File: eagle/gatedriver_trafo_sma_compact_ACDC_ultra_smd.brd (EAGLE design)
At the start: 101.9 x 165.1 mm, 90 parts, among them K1 G5V-2, X4 BU-SMA-V

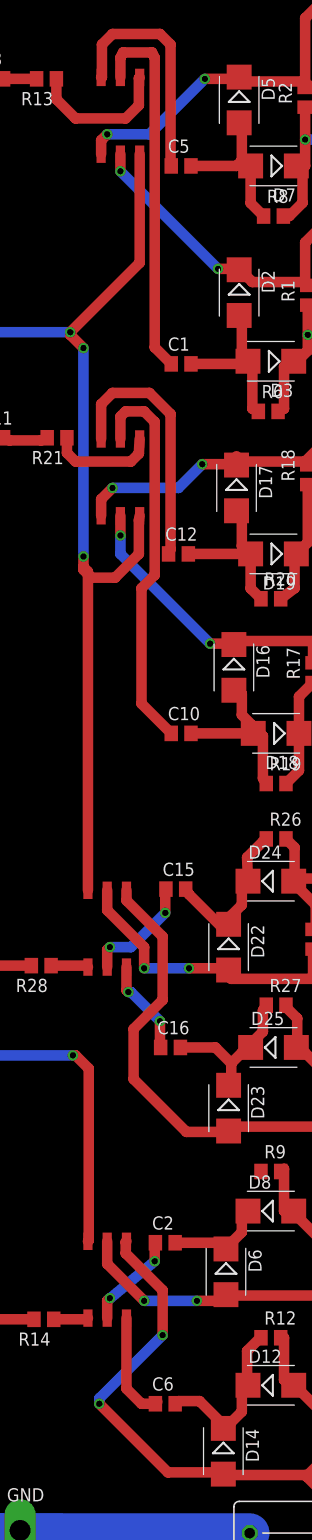
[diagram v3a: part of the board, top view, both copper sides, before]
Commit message: add tplace trafo
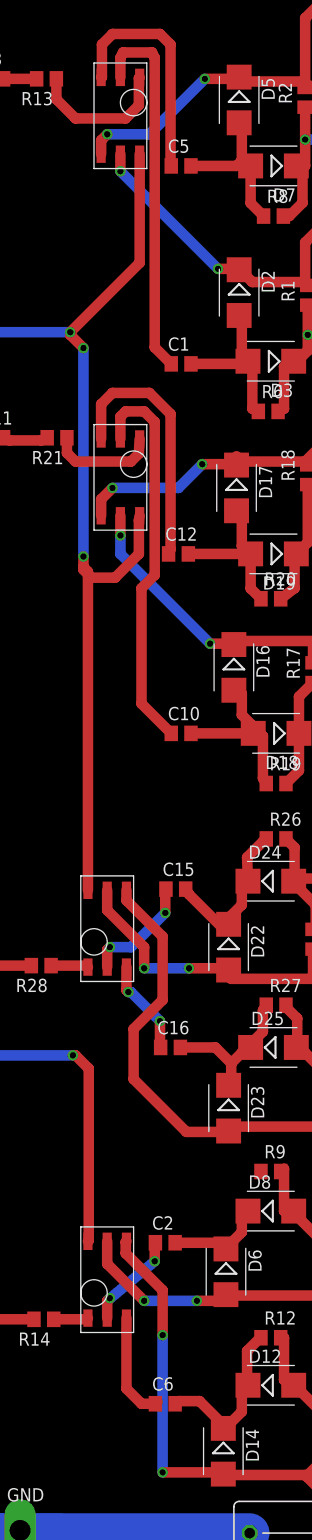
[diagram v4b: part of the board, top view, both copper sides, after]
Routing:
- net N$24: track 89.3 -> 84.5 mm
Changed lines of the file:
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@@
 <wire x1="75.184" y1="8.382" x2="74.93" y2="7.874" width="1.016" layer="1"/>
 <wire x1="88.392" y1="7.874" x2="87.884" y2="7.874" width="1.016" layer="16"/>
-<wire x1="50.292" y1="20.32" x2="56.896" y2="13.716" width="1.016" layer="1"/>
-<wire x1="56.896" y1="13.716" x2="62.5155" y2="13.716" width="1.016" layer="1"/>
+<wire x1="56.388" y1="13.716" x2="62.5155" y2="13.716" width="1.016" layer="1"/>
 <wire x1="62.5155" y1="13.716" x2="62.74119375" y2="13.49030625" width="1.016" layer="1"/>
 <wire x1="75.463" y1="18.745" x2="75.133" y2="18.745" width="1.016" layer="1"/>
@@
 <wire x1="71.628" y1="14.732" x2="70.231" y2="13.335" width="1.016" layer="1"/>
 <wire x1="87.884" y1="7.874" x2="87.884" y2="13.97" width="1.4224" layer="1"/>
-<via x="50.292" y="20.32" extent="1-16" drill="0.6" shape="square"/>
-<wire x1="50.292" y1="20.32" x2="50.292" y2="20.828" width="1.016" layer="16"/>
-<wire x1="50.292" y1="20.828" x2="56.388" y2="26.924" width="1.016" layer="16"/>
+<via x="56.388" y="13.716" extent="1-16" drill="0.6" shape="square"/>
+<wire x1="56.388" y1="13.716" x2="56.388" y2="26.924" width="1.016" layer="16"/>
 <via x="56.388" y="26.924" extent="1-16" drill="0.6" shape="square"/>
 <wire x1="56.388" y1="26.924" x2="56.388" y2="31.242" width="1.016" layer="1"/>

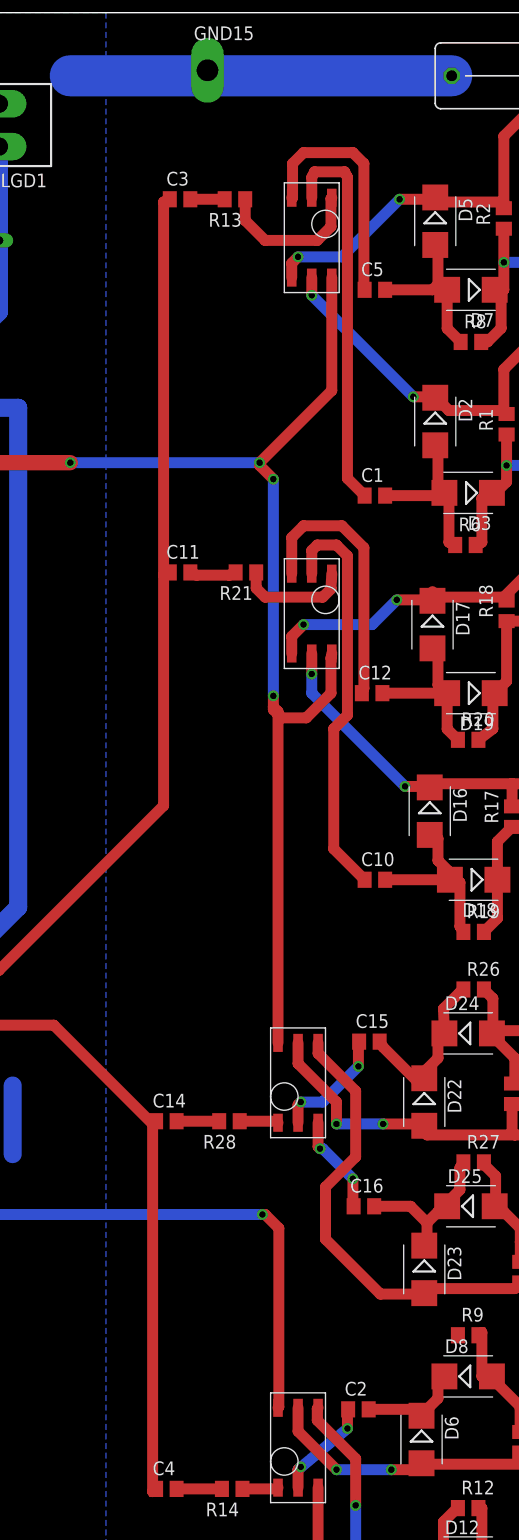
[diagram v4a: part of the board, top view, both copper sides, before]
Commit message: Fix negative rail problems
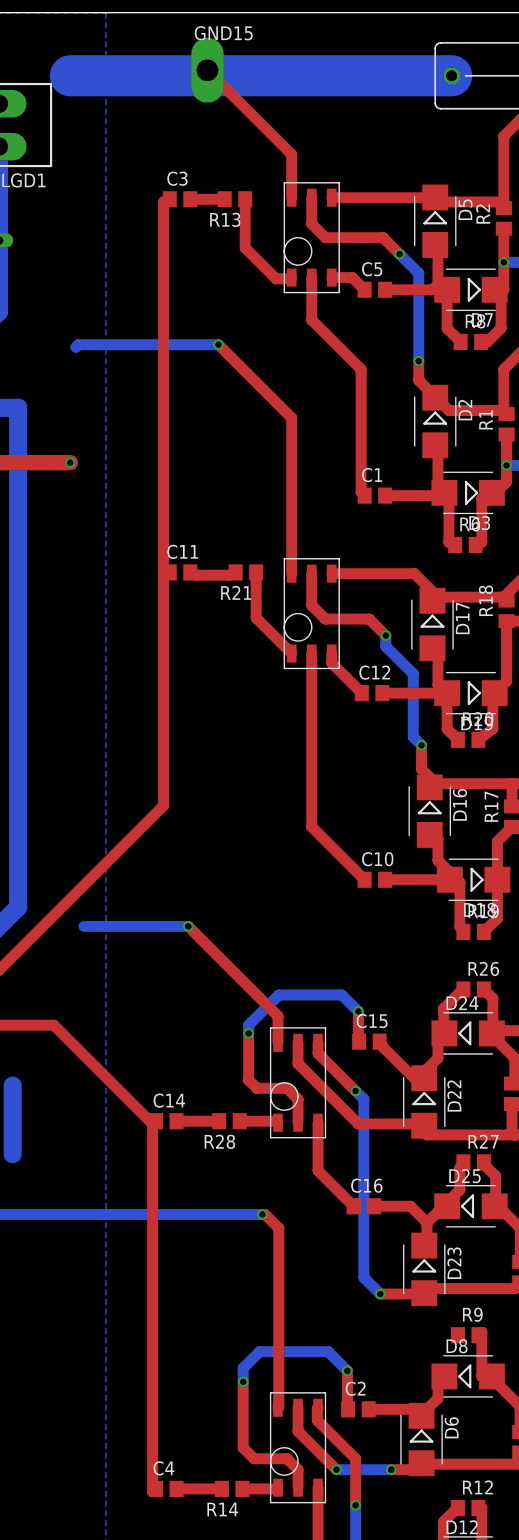
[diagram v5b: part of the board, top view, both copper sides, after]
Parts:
- D14, D16, D17, D2, D22, D23, D5, D6: value 4742 -> 1SMB5918BT3G
- R10, R11, R15, R16, R22, R23, R4, R7: value 1M -> 10M
- turned U$1 to 90 degrees
- turned U$8 to 90 degrees
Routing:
- net GND: track 272.9 -> 246.7 mm, vias 6 -> 5
- net N$29: track 24.8 -> 4.82 mm
- net N$22: track 10.1 -> 29.6 mm
- net N$7: track 22.4 -> 3.51 mm
- net N$40: track 11.0 -> 27.3 mm
- net N$28: track 37.8 -> 23.0 mm
- net N$5: track 35.9 -> 22.2 mm
- net N$18: track 102.3 -> 111.9 mm
- net N$33: track 97.3 -> 105.7 mm
- net N$17: track 88.1 -> 80.6 mm, vias 2 -> 0
- net N$32: track 103.0 -> 97.0 mm, vias 4 -> 2
- net N$3: track 13.9 -> 10.0 mm
- net N$51: track 100.9 -> 98.6 mm, vias 0 -> 2
- net N$37: track 10.5 -> 8.87 mm
- net N$46: track 93.7 -> 92.5 mm, vias 2 -> 0
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
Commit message: Fix gate driver missing trace, make changes to code for wei
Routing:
- net N$25: track 10.0 -> 14.3 mm
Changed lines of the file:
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@@
 <wire x1="64.008" y1="38.862" x2="64.602" y2="38.862" width="1.016" layer="1"/>
 <wire x1="62.992" y1="35.814" x2="62.484" y2="35.22" width="1.016" layer="1"/>
-<wire x1="64.602" y1="38.862" x2="65.852" y2="42.672" width="0" layer="19" extent="1-1"/>
+<wire x1="64.602" y1="38.862" x2="64.602" y2="41.422" width="1.016" layer="1"/>
+<wire x1="64.602" y1="41.422" x2="65.852" y2="42.672" width="1.016" layer="1"/>
 </signal>
 <signal name="N$27">

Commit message: Component value changes for gate driver with new fets (VN2450)
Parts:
- C1, C10, C11, C12, C14, C15, C16, C2, C3, C4, C5, C6: value .22u -> 1u
- R13, R14, R28: value 50 -> 10
- R21: value 50 -> 1u
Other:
- board text added: "Requires conformal coating"
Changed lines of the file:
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@@
 <hole x="6.858" y="4.572" drill="3.7973"/>
 <hole x="5.842" y="159.258" drill="3.7973"/>
+<text x="2.032" y="40.386" size="1.778" layer="21">Requires conformal coating</text>
 </plain>
 <attributes>
@@
 <attribute name="OC_FARNELL" value="unknown" x="23.368" y="154.686" size="1.778" layer="27" rot="R90" display="off"/>
 </element>
-<element name="C1" library="resistor" package="C0805" value=".22u" x="58.166" y="120.396"/>
-<element name="C3" library="resistor" package="C0805" value=".22u" x="40.132" y="147.828"/>
+<element name="C1" library="resistor" package="C0805" value="1u" x="58.166" y="120.396"/>
+<element name="C3" library="resistor" package="C0805" value="1u" x="40.132" y="147.828"/>
 <element name="U$3" library="texas" package="DIL08" value="UCC27425" x="18.288" y="75.438" rot="R270"/>
-<element name="C4" library="resistor" package="C0805" value=".22u" x="38.862" y="28.448"/>
+<element name="C4" library="resistor" package="C0805" value="1u" x="38.862" y="28.448"/>
 <element name="K1" library="relay" package="G5V-2" value="G5V-2" x="18.288" y="127.254" rot="R270">
 <attribute name="OC_NEWARK" value="78K5703" x="18.288" y="127.254" size="1.778" layer="27" rot="R270" display="off"/>
@@
 <element name="D11" library="diode" package="DO35-10" value="1N4148DO35-10" x="18.288" y="144.018"/>
 <element name="U$1" library="trafo" package="SMD6" value="DA-2320SMD6" x="52.324" y="144.272" rot="R90"/>
-<element name="C5" library="resistor" package="C0805" value=".22u" x="58.166" y="139.446"/>
+<element name="C5" library="resistor" package="C0805" value="1u" x="58.166" y="139.446"/>
 <element name="R4" library="rcl" package="R2512" value="10M" x="84.328" y="146.05" rot="R270"/>
 <element name="R7" library="rcl" package="R2512" value="10M" x="84.074" y="127.254" rot="R270"/>
-<element name="C2" library="resistor" package="C0805" value=".22u" x="56.642" y="35.814"/>
+<element name="C2" library="resistor" package="C0805" value="1u" x="56.642" y="35.814"/>
 <element name="U$2" library="transistor-fet" package="SOT89-BCE" value="VN2450" x="77.216" y="33.274" rot="R180"/>
 <element name="U$6" library="transistor-fet" package="SOT89-BCE" value="VN2450" x="76.962" y="16.764" rot="R180"/>
 <element name="U$7" library="trafo" package="SMD6" value="DA-2320SMD6" x="51.054" y="32.258" rot="R90"/>
-<element name="C6" library="resistor" package="C0805" value=".22u" x="56.642" y="20.32"/>
+<element name="C6" library="resistor" package="C0805" value="1u" x="56.642" y="20.32"/>
 <element name="R10" library="rcl" package="R2512" value="10M" x="83.82" y="34.798" rot="R90"/>
 <element name="R11" library="rcl" package="R2512" value="10M" x="83.82" y="17.78" rot="R90"/>
@@
 <element name="R9" library="rcl" package="R0805" value="10" x="66.802" y="42.672"/>
 <element name="R12" library="rcl" package="R0805" value="10" x="66.802" y="26.67"/>
-<element name="R13" library="rcl" package="R0805" value="50" x="45.212" y="147.828" rot="R180"/>
-<element name="R14" library="rcl" package="R0805" value="50" x="44.958" y="28.448" rot="R180"/>
+<element name="R13" library="rcl" package="R0805" value="10" x="45.212" y="147.828" rot="R180"/>
+<element name="R14" library="rcl" package="R0805" value="10" x="44.958" y="28.448" rot="R180"/>
 <element name="C8" library="resistor" package="C102-064X133" value="10p" x="70.358" y="159.258" rot="R180"/>
 <element name="HV2" library="testpad" package="P1-20Y" value="TPPAD1-20Y" x="87.884" y="7.874">
@@
 <attribute name="TP_SIGNAL_NAME" value="" x="74.676" y="92.964" size="1.778" layer="27" display="off"/>
 </element>
-<element name="C10" library="resistor" package="C0805" value=".22u" x="58.166" y="84.836"/>
-<element name="C11" library="resistor" package="C0805" value=".22u" x="40.132" y="113.284"/>
+<element name="C10" library="resistor" package="C0805" value="1u" x="58.166" y="84.836"/>
+<element name="C11" library="resistor" package="C0805" value="1u" x="40.132" y="113.284"/>
 <element name="U$8" library="trafo" package="SMD6" value="DA-2320SMD6" x="52.324" y="109.474" rot="R90"/>
-<element name="C12" library="resistor" package="C0805" value=".22u" x="57.912" y="102.108"/>
+<element name="C12" library="resistor" package="C0805" value="1u" x="57.912" y="102.108"/>
 <element name="R15" library="rcl" package="R2512" value="10M" x="84.074" y="110.236" rot="R90"/>
 <element name="R16" library="rcl" package="R2512" value="10M" x="84.074" y="90.678" rot="R90"/>
@@
 <element name="R19" library="rcl" package="R0805" value="10" x="67.31" y="80.01"/>
 <element name="R20" library="rcl" package="R0805" value="10" x="66.802" y="97.79"/>
-<element name="R21" library="rcl" package="R0805" value="50" x="46.228" y="113.284" rot="R180"/>
+<element name="R21" library="rcl" package="R0805" value="1u" x="46.228" y="113.284" rot="R180"/>
 <element name="D18" library="diode" package="SMB" value="" x="67.31" y="84.836" rot="R180"/>
 <element name="D19" library="diode" package="SMB" value="" x="67.056" y="102.108" rot="R180"/>
-<element name="C14" library="resistor" package="C0805" value=".22u" x="38.862" y="62.484"/>
-<element name="C15" library="resistor" package="C0805" value=".22u" x="57.658" y="69.85"/>
+<element name="C14" library="resistor" package="C0805" value="1u" x="38.862" y="62.484"/>
+<element name="C15" library="resistor" package="C0805" value="1u" x="57.658" y="69.85"/>
 <element name="U$11" library="transistor-fet" package="SOT89-BCE" value="VN2450" x="76.962" y="66.294" rot="R180"/>
 <element name="U$12" library="transistor-fet" package="SOT89-BCE" value="VN2450" x="77.216" y="48.768" rot="R180"/>
 <element name="U$13" library="trafo" package="SMD6" value="DA-2320SMD6" x="51.054" y="66.04" rot="R90"/>
-<element name="C16" library="resistor" package="C0805" value=".22u" x="57.15" y="54.61"/>
+<element name="C16" library="resistor" package="C0805" value="1u" x="57.15" y="54.61"/>
 <element name="R22" library="rcl" package="R2512" value="10M" x="84.074" y="67.564" rot="R90"/>
 <element name="R23" library="rcl" package="R2512" value="10M" x="83.82" y="50.546" rot="R90"/>
@@
 <element name="R26" library="rcl" package="R0805" value="10" x="67.31" y="74.676"/>
 <element name="R27" library="rcl" package="R0805" value="10" x="67.31" y="58.674"/>
-<element name="R28" library="rcl" package="R0805" value="50" x="44.704" y="62.484" rot="R180"/>
+<element name="R28" library="rcl" package="R0805" value="10" x="44.704" y="62.484" rot="R180"/>
 <element name="D24" library="diode" package="SMB" value="" x="66.802" y="70.612"/>
 <element name="D25" library="diode" package="SMB" value="" x="67.056" y="54.61"/>

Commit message: Changes for CTIA integration
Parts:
- C7: value (none) -> 10n
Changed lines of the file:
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@@
 <element name="D6" library="diode" package="SMB" value="1SMB5918BT3G" x="62.484" y="33.02" rot="R270"/>
 <element name="D14" library="diode" package="SMB" value="1SMB5918BT3G" x="62.23" y="15.748" rot="R270"/>
-<element name="C7" library="rcl" package="C050-030X075" value="" x="6.858" y="141.478" rot="R270"/>
+<element name="C7" library="rcl" package="C050-030X075" value="10n" x="6.858" y="141.478" rot="R270"/>
 <element name="R1" library="rcl" package="R0805" value="100k" x="70.358" y="127" rot="R90"/>
 <element name="R2" library="rcl" package="R0805" value="100k" x="70.104" y="146.05" rot="R90"/>
